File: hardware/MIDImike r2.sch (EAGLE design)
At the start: 8 parts, among them SW1 PUSH-BTN, SW2 SH-7030TB

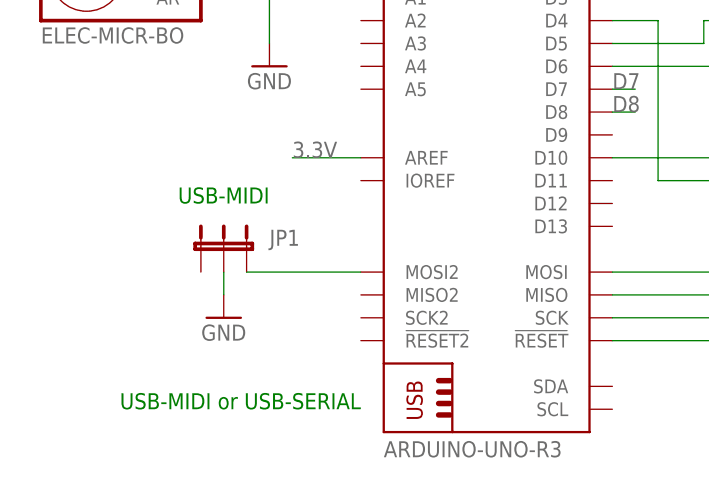
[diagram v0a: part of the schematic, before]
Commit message: fix so that USB-MIDI connects to MISO2
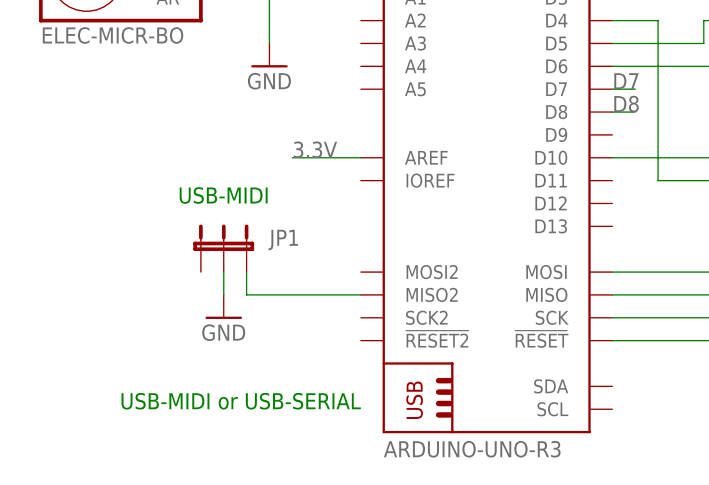
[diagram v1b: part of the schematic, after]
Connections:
- net N$3: now also PCB2.IO.MISO2; no longer PCB2.IO.MOSI2
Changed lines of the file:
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@@
-</segment>
-</net>
-<net name="N$3" class="0">
-<segment>
-<pinref part="PCB2" gate=".IO" pin="MOSI2"/>
-<pinref part="JP1" gate="1" pin="3"/>
-<wire x1="55.88" y1="81.28" x2="43.18" y2="81.28" width="0.1524" layer="91"/>
 </segment>
 </net>
@@
 </segment>
 </net>
+<net name="N$3" class="0">
+<segment>
+<pinref part="JP1" gate="1" pin="3"/>
+<wire x1="43.18" y1="81.28" x2="43.18" y2="78.74" width="0.1524" layer="91"/>
+<pinref part="PCB2" gate=".IO" pin="MISO2"/>
+<wire x1="43.18" y1="78.74" x2="55.88" y2="78.74" width="0.1524" layer="91"/>
+</segment>
+</net>
